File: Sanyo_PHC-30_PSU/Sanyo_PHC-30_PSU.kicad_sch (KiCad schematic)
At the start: 17 parts, among them J1 To Data Recorder, J2 12VDC In, J3 To Motherboard, J4 Ground Strap, U1 PSU2-5, U2 NKE1212SC

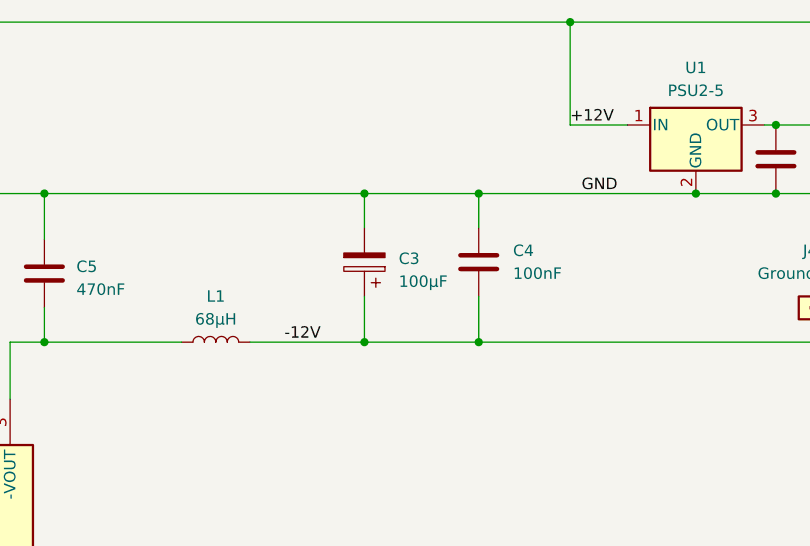
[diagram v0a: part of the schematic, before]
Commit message: Fixed C3 orientation
+ve leg of electrolytic should be connected to GND and -ve leg to -12V ... GND is more positive than -12V, duh
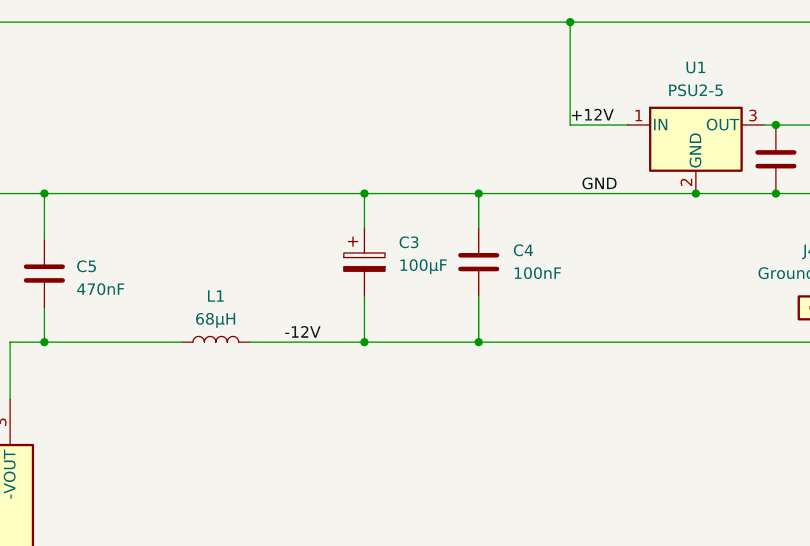
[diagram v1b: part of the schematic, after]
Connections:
- net -12V: now also C3.2; no longer C3.1
- net GND: now also C3.1; no longer C3.2
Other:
- moved on the sheet: C3
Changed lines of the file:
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@@
 		)
 		(instances
-			(project ""
+			(project "Sanyo_PHC-30_PSU"
 				(path "/5701d330-320f-44bd-abfd-142c6c413949"
 					(reference "H4")
@@
 		)
 		(instances
-			(project ""
+			(project "Sanyo_PHC-30_PSU"
 				(path "/5701d330-320f-44bd-abfd-142c6c413949"
 					(reference "H3")
@@
 	(symbol
 		(lib_id "Device:C_Polarized")
-		(at 123.19 69.85 180)
+		(at 123.19 69.85 0)
 		(unit 1)
 		(exclude_from_sim no)
@@
 		(fields_autoplaced yes)
 		(property "Reference" "C3"
-			(at 127 69.4689 0)
-			(effects
-				(font
-					(size 1.27 1.27)
-				)
-				(justify right)
+			(at 127 67.6909 0)
+			(effects
+				(font
+					(size 1.27 1.27)
+				)
+				(justify left)
 			)
 		)
 		(property "Value" "100µF"
-			(at 127 72.0089 0)
-			(effects
-				(font
-					(size 1.27 1.27)
-				)
-				(justify right)
+			(at 127 70.2309 0)
+			(effects
+				(font
+					(size 1.27 1.27)
+				)
+				(justify left)
 			)
 		)
 		(property "Footprint" "Capacitor_THT:CP_Radial_D5.0mm_P2.50mm"
-			(at 122.2248 66.04 0)
+			(at 124.1552 73.66 0)
 			(effects
 				(font
@@
 		)
 		(instances
-			(project ""
+			(project "Sanyo_PHC-30_PSU"
 				(path "/5701d330-320f-44bd-abfd-142c6c413949"
 					(reference "C3")
@@
 		)
 		(instances
-			(project ""
+			(project "Sanyo_PHC-30_PSU"
 				(path "/5701d330-320f-44bd-abfd-142c6c413949"
 					(reference "U2")
@@
 		)
 		(instances
-			(project ""
+			(project "Sanyo_PHC-30_PSU"
 				(path "/5701d330-320f-44bd-abfd-142c6c413949"
 					(reference "C1")
@@
 		)
 		(instances
-			(project ""
+			(project "Sanyo_PHC-30_PSU"
 				(path "/5701d330-320f-44bd-abfd-142c6c413949"
 					(reference "J4")
@@
 		)
 		(instances
-			(project ""
+			(project "Sanyo_PHC-30_PSU"
 				(path "/5701d330-320f-44bd-abfd-142c6c413949"
 					(reference "J2")
@@
 		)
 		(instances
-			(project ""
+			(project "Sanyo_PHC-30_PSU"
 				(path "/5701d330-320f-44bd-abfd-142c6c413949"
 					(reference "J3")
@@
 		)
 		(instances
-			(project ""
+			(project "Sanyo_PHC-30_PSU"
 				(path "/5701d330-320f-44bd-abfd-142c6c413949"
 					(reference "U1")
@@
 		)
 		(instances
-			(project ""
+			(project "Sanyo_PHC-30_PSU"
 				(path "/5701d330-320f-44bd-abfd-142c6c413949"
 					(reference "H2")
@@
 		)
 		(instances
-			(project ""
+			(project "Sanyo_PHC-30_PSU"
 				(path "/5701d330-320f-44bd-abfd-142c6c413949"
 					(reference "L1")
@@
 		)
 		(instances
-			(project ""
+			(project "Sanyo_PHC-30_PSU"
 				(path "/5701d330-320f-44bd-abfd-142c6c413949"
 					(reference "H1")
@@
 		)
 		(instances
-			(project ""
+			(project "Sanyo_PHC-30_PSU"
 				(path "/5701d330-320f-44bd-abfd-142c6c413949"
 					(reference "C2")
@@
 		)
 		(instances
-			(project ""
+			(project "Sanyo_PHC-30_PSU"
 				(path "/5701d330-320f-44bd-abfd-142c6c413949"
 					(reference "F1")
